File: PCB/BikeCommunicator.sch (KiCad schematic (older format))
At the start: 26 parts, among them J1 Barrel_Jack_Switch, J2 USB_B_Micro, J3 Conn_01x04, J4 Conn_01x02, SW1 SW_SPST_LED, SW2 SW_SPST_LED, SW3 SW_SPST_LED, SW4 SW_SPST_LED, SW5 SW_DPDT_x2, U1 HW-108_DC-DC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

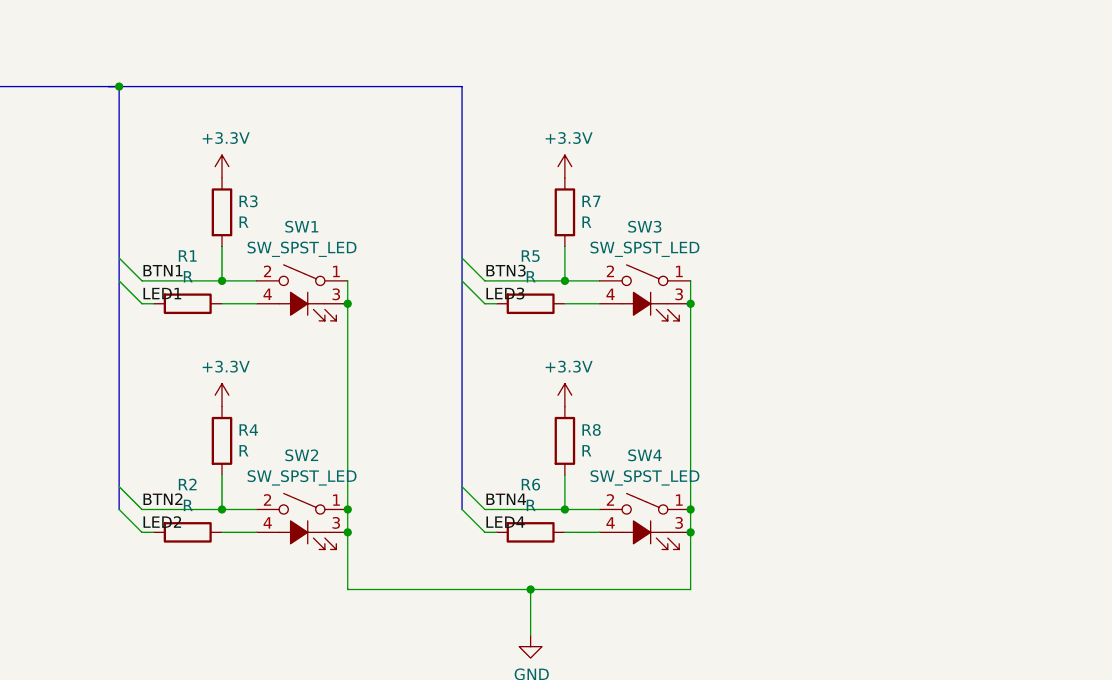
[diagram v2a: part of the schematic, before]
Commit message: Added resistor values
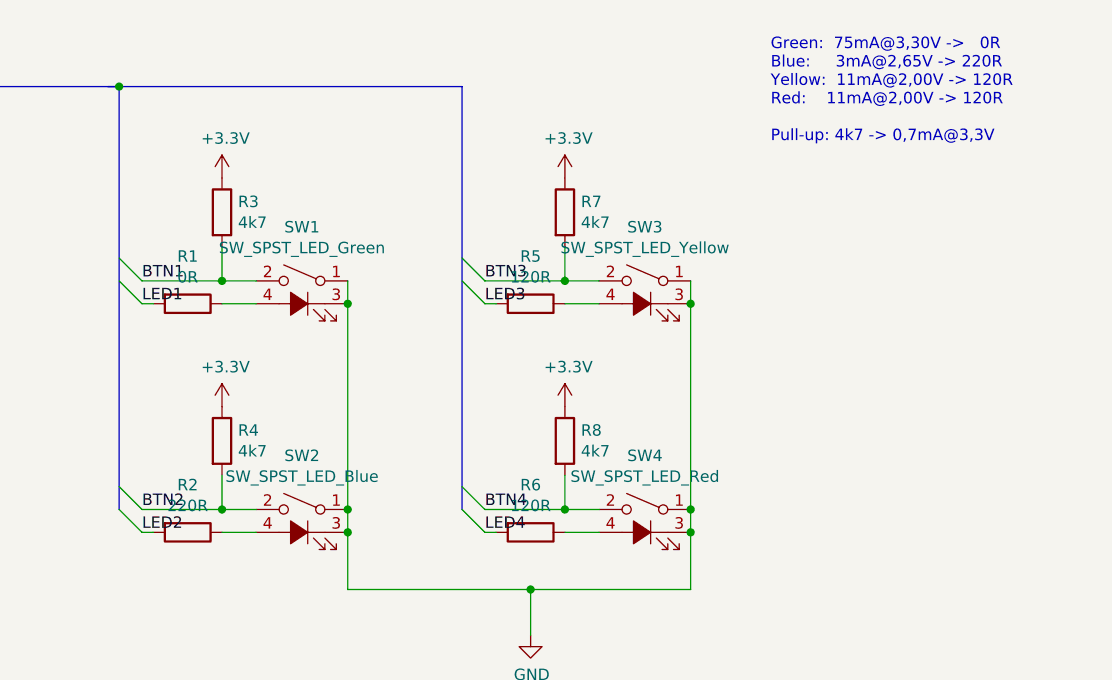
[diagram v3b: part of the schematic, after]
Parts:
- R1: value R -> 0R
- R2: value R -> 220R
- R3, R4, R7, R8: value R -> 4k7
- R5, R6: value R -> 120R
- SW1: value SW_SPST_LED -> SW_SPST_LED_Green
- SW2: value SW_SPST_LED -> SW_SPST_LED_Blue
- SW3: value SW_SPST_LED -> SW_SPST_LED_Yellow
- SW4: value SW_SPST_LED -> SW_SPST_LED_Red
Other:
- note added: "Green: 75mA@3,30V -> 0R\nBlue: 3mA@2,65V -> 220R\nYellow: 11mA@2,00V -> 120R\nRed: 11mA@2,00V -> 120R\n\nPull-up: 4k7 -> 0,7mA@3,3V"
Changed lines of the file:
@@
 P 7500 1750
 F 0 "SW1" H 7500 2085 50  0000 C CNN
-F 1 "SW_SPST_LED" H 7500 1994 50  0000 C CNN
+F 1 "SW_SPST_LED_Green" H 7500 1994 50  0000 C CNN
 F 2 "Buttons_Switches_Keyboard:SW_Cherry_MX1A_LED_1.00u_PCB" H 7500 2050 50  0001 C CNN
 F 3 "~" H 7500 2050 50  0001 C CNN
@@
 P 9000 1750
 F 0 "SW3" H 9000 2085 50  0000 C CNN
-F 1 "SW_SPST_LED" H 9000 1994 50  0000 C CNN
+F 1 "SW_SPST_LED_Yellow" H 9000 1994 50  0000 C CNN
 F 2 "Buttons_Switches_Keyboard:SW_Cherry_MX1A_LED_1.00u_PCB" H 9000 2050 50  0001 C CNN
 F 3 "~" H 9000 2050 50  0001 C CNN
@@
 P 7500 2750
 F 0 "SW2" H 7500 3085 50  0000 C CNN
-F 1 "SW_SPST_LED" H 7500 2994 50  0000 C CNN
+F 1 "SW_SPST_LED_Blue" H 7500 2994 50  0000 C CNN
 F 2 "Buttons_Switches_Keyboard:SW_Cherry_MX1A_LED_1.00u_PCB" H 7500 3050 50  0001 C CNN
 F 3 "~" H 7500 3050 50  0001 C CNN
@@
 P 9000 2750
 F 0 "SW4" H 9000 3085 50  0000 C CNN
-F 1 "SW_SPST_LED" H 9000 2994 50  0000 C CNN
+F 1 "SW_SPST_LED_Red" H 9000 2994 50  0000 C CNN
 F 2 "Buttons_Switches_Keyboard:SW_Cherry_MX1A_LED_1.00u_PCB" H 9000 3050 50  0001 C CNN
 F 3 "~" H 9000 3050 50  0001 C CNN
@@
 P 7150 1350
 F 0 "R3" H 7220 1396 50  0000 L CNN
-F 1 "R" H 7220 1305 50  0000 L CNN
+F 1 "4k7" H 7220 1305 50  0000 L CNN
 F 2 "Resistor_THT:R_Axial_DIN0207_L6.3mm_D2.5mm_P7.62mm_Horizontal" V 7080 1350 50  0001 C CNN
 F 3 "~" H 7150 1350 50  0001 C CNN
@@
 P 7150 2350
 F 0 "R4" H 7220 2396 50  0000 L CNN
-F 1 "R" H 7220 2305 50  0000 L CNN
+F 1 "4k7" H 7220 2305 50  0000 L CNN
 F 2 "Resistor_THT:R_Axial_DIN0207_L6.3mm_D2.5mm_P7.62mm_Horizontal" V 7080 2350 50  0001 C CNN
 F 3 "~" H 7150 2350 50  0001 C CNN
@@
 P 8650 1350
 F 0 "R7" H 8720 1396 50  0000 L CNN
-F 1 "R" H 8720 1305 50  0000 L CNN
+F 1 "4k7" H 8720 1305 50  0000 L CNN
 F 2 "Resistor_THT:R_Axial_DIN0207_L6.3mm_D2.5mm_P7.62mm_Horizontal" V 8580 1350 50  0001 C CNN
 F 3 "~" H 8650 1350 50  0001 C CNN
@@
 P 8650 2350
 F 0 "R8" H 8720 2396 50  0000 L CNN
-F 1 "R" H 8720 2305 50  0000 L CNN
+F 1 "4k7" H 8720 2305 50  0000 L CNN
 F 2 "Resistor_THT:R_Axial_DIN0207_L6.3mm_D2.5mm_P7.62mm_Horizontal" V 8580 2350 50  0001 C CNN
 F 3 "~" H 8650 2350 50  0001 C CNN
@@
 P 7000 1750
 F 0 "R1" V 6793 1750 50  0000 C CNN
-F 1 "R" V 6884 1750 50  0000 C CNN
+F 1 "0R" V 6884 1750 50  0000 C CNN
 F 2 "Resistor_THT:R_Axial_DIN0207_L6.3mm_D2.5mm_P7.62mm_Horizontal" V 6930 1750 50  0001 C CNN
 F 3 "~" H 7000 1750 50  0001 C CNN
@@
 P 7000 2750
 F 0 "R2" V 6793 2750 50  0000 C CNN
-F 1 "R" V 6884 2750 50  0000 C CNN
+F 1 "220R" V 6884 2750 50  0000 C CNN
 F 2 "Resistor_THT:R_Axial_DIN0207_L6.3mm_D2.5mm_P7.62mm_Horizontal" V 6930 2750 50  0001 C CNN
 F 3 "~" H 7000 2750 50  0001 C CNN
@@
 P 8500 1750
 F 0 "R5" V 8293 1750 50  0000 C CNN
-F 1 "R" V 8384 1750 50  0000 C CNN
+F 1 "120R" V 8384 1750 50  0000 C CNN
 F 2 "Resistor_THT:R_Axial_DIN0207_L6.3mm_D2.5mm_P7.62mm_Horizontal" V 8430 1750 50  0001 C CNN
 F 3 "~" H 8500 1750 50  0001 C CNN
@@
 P 8500 2750
 F 0 "R6" V 8293 2750 50  0000 C CNN
-F 1 "R" V 8384 2750 50  0000 C CNN
+F 1 "120R" V 8384 2750 50  0000 C CNN
 F 2 "Resistor_THT:R_Axial_DIN0207_L6.3mm_D2.5mm_P7.62mm_Horizontal" V 8430 2750 50  0001 C CNN
 F 3 "~" H 8500 2750 50  0001 C CNN
@@
 Wire Wire Line
 	9300 4500 9500 4500
-Wire Bus Line
-	8200 800  8200 2650
-Wire Bus Line
-	6700 800  6700 2650
-Wire Bus Line
-	4550 800  4550 5250
 Connection ~ 9300 4500
 $Comp
@@
 $EndComp
 Connection ~ 8900 4500
+Wire Bus Line
+	8200 800  8200 2650
+Wire Bus Line
+	6700 800  6700 2650
+Wire Bus Line
+	4550 800  4550 5250
+Text Notes 9550 1050 0    50   ~ 0
+Green:  75mA@3,30V ->   0R\nBlue:     3mA@2,65V -> 220R\nYellow:  11mA@2,00V -> 120R\nRed:    11mA@2,00V -> 120R\n\nPull-up: 4k7 -> 0,7mA@3,3V
 $EndSCHEMATC

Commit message: SMD components on PCB, fabrication files...
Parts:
- BT1: footprint Connector_Wire:SolderWirePad_1x02_P7.62mm_Drill2mm -> Connector_Wire:SolderWirePad_1x02_P3.81mm_Drill1mm
- D1, D2: footprint Diodes_THT:D_A-405_P7.62mm_Horizontal -> Diodes_SMD:D_SMA
- R1, R2, R3, R4, R5, R6, R7, R8: footprint Resistor_THT:R_Axial_DIN0207_L6.3mm_D2.5mm_P7.62mm_Horizontal -> Resistors_SMD:R_1206
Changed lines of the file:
@@
 F 0 "R3" H 7220 1396 50  0000 L CNN
 F 1 "4k7" H 7220 1305 50  0000 L CNN
-F 2 "Resistor_THT:R_Axial_DIN0207_L6.3mm_D2.5mm_P7.62mm_Horizontal" V 7080 1350 50  0001 C CNN
+F 2 "Resistors_SMD:R_1206" V 7080 1350 50  0001 C CNN
 F 3 "~" H 7150 1350 50  0001 C CNN
 	1    7150 1350
@@
 F 0 "R4" H 7220 2396 50  0000 L CNN
 F 1 "4k7" H 7220 2305 50  0000 L CNN
-F 2 "Resistor_THT:R_Axial_DIN0207_L6.3mm_D2.5mm_P7.62mm_Horizontal" V 7080 2350 50  0001 C CNN
+F 2 "Resistors_SMD:R_1206" V 7080 2350 50  0001 C CNN
 F 3 "~" H 7150 2350 50  0001 C CNN
 	1    7150 2350
@@
 F 0 "R7" H 8720 1396 50  0000 L CNN
 F 1 "4k7" H 8720 1305 50  0000 L CNN
-F 2 "Resistor_THT:R_Axial_DIN0207_L6.3mm_D2.5mm_P7.62mm_Horizontal" V 8580 1350 50  0001 C CNN
+F 2 "Resistors_SMD:R_1206" V 8580 1350 50  0001 C CNN
 F 3 "~" H 8650 1350 50  0001 C CNN
 	1    8650 1350
@@
 F 0 "R8" H 8720 2396 50  0000 L CNN
 F 1 "4k7" H 8720 2305 50  0000 L CNN
-F 2 "Resistor_THT:R_Axial_DIN0207_L6.3mm_D2.5mm_P7.62mm_Horizontal" V 8580 2350 50  0001 C CNN
+F 2 "Resistors_SMD:R_1206" V 8580 2350 50  0001 C CNN
 F 3 "~" H 8650 2350 50  0001 C CNN
 	1    8650 2350
@@
 F 0 "R1" V 6793 1750 50  0000 C CNN
 F 1 "0R" V 6884 1750 50  0000 C CNN
-F 2 "Resistor_THT:R_Axial_DIN0207_L6.3mm_D2.5mm_P7.62mm_Horizontal" V 6930 1750 50  0001 C CNN
+F 2 "Resistors_SMD:R_1206" V 6930 1750 50  0001 C CNN
 F 3 "~" H 7000 1750 50  0001 C CNN
 	1    7000 1750
@@
 F 0 "R2" V 6793 2750 50  0000 C CNN
 F 1 "220R" V 6884 2750 50  0000 C CNN
-F 2 "Resistor_THT:R_Axial_DIN0207_L6.3mm_D2.5mm_P7.62mm_Horizontal" V 6930 2750 50  0001 C CNN
+F 2 "Resistors_SMD:R_1206" V 6930 2750 50  0001 C CNN
 F 3 "~" H 7000 2750 50  0001 C CNN
 	1    7000 2750
@@
 F 0 "R5" V 8293 1750 50  0000 C CNN
 F 1 "120R" V 8384 1750 50  0000 C CNN
-F 2 "Resistor_THT:R_Axial_DIN0207_L6.3mm_D2.5mm_P7.62mm_Horizontal" V 8430 1750 50  0001 C CNN
+F 2 "Resistors_SMD:R_1206" V 8430 1750 50  0001 C CNN
 F 3 "~" H 8500 1750 50  0001 C CNN
 	1    8500 1750
@@
 F 0 "R6" V 8293 2750 50  0000 C CNN
 F 1 "120R" V 8384 2750 50  0000 C CNN
-F 2 "Resistor_THT:R_Axial_DIN0207_L6.3mm_D2.5mm_P7.62mm_Horizontal" V 8430 2750 50  0001 C CNN
+F 2 "Resistors_SMD:R_1206" V 8430 2750 50  0001 C CNN
 F 3 "~" H 8500 2750 50  0001 C CNN
 	1    8500 2750
@@
 F 0 "BT1" H 2418 2646 50  0000 L CNN
 F 1 "Battery_Cell" H 2418 2555 50  0000 L CNN
-F 2 "Connector_Wire:SolderWirePad_1x02_P7.62mm_Drill2mm" V 2300 2610 50  0001 C CNN
+F 2 "Connector_Wire:SolderWirePad_1x02_P3.81mm_Drill1mm" V 2300 2610 50  0001 C CNN
 F 3 "~" V 2300 2610 50  0001 C CNN
 	1    2300 2550
@@
 F 0 "D1" H 6800 4383 50  0000 C CNN
 F 1 "D" H 6800 4474 50  0000 C CNN
-F 2 "Diodes_THT:D_A-405_P7.62mm_Horizontal" H 6800 4600 50  0001 C CNN
+F 2 "Diodes_SMD:D_SMA" H 6800 4600 50  0001 C CNN
 F 3 "~" H 6800 4600 50  0001 C CNN
 	1    6800 4600
@@
 F 0 "D2" H 6850 5033 50  0000 C CNN
 F 1 "D" H 6850 5124 50  0000 C CNN
-F 2 "Diodes_THT:D_A-405_P7.62mm_Horizontal" H 6850 5250 50  0001 C CNN
+F 2 "Diodes_SMD:D_SMA" H 6850 5250 50  0001 C CNN
 F 3 "~" H 6850 5250 50  0001 C CNN
 	1    6850 5250
@@
 $EndComp
 Connection ~ 8900 4500
+Text Notes 9550 1050 0    50   ~ 0
+Green:  75mA@3,30V ->   0R\nBlue:     3mA@2,65V -> 220R\nYellow:  11mA@2,00V -> 120R\nRed:    11mA@2,00V -> 120R\n\nPull-up: 4k7 -> 0,7mA@3,3V
 Wire Bus Line
 	8200 800  8200 2650
@@
 Wire Bus Line
 	4550 800  4550 5250
-Text Notes 9550 1050 0    50   ~ 0
-Green:  75mA@3,30V ->   0R\nBlue:     3mA@2,65V -> 220R\nYellow:  11mA@2,00V -> 120R\nRed:    11mA@2,00V -> 120R\n\nPull-up: 4k7 -> 0,7mA@3,3V
 $EndSCHEMATC
